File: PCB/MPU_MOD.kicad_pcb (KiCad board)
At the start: 8 copper layers, 45 x 70 mm, 305 parts, among them J1 SJ3-35024K-SMT-TR, J2 2-1734248-0, J501 MEM2090-00-145-00-A_REVA, J701 FTSH-107-01-L-DV-K-A, J801 USB4215-03-A_REVA, J901 73412-0110, U1 IS21ES08GA-JQLI-TR, U201 STC3115IQT, U203 STPMIC1APQR, U3 BQ24298RTWR, U301 STM32MP157FABx, U401 MT41K256M16TW-107_P, U502 HSP051-4M10, U503 HSP051-4M10, U701 HSP051-4M10, U702 HSP051-4M10, U801 FUSB302BMPX, U802 HSP051-4M10, U901 LBEE5PK2AE-771, Y601 NX2012SA-32.768K, Y701 ECS-2520MVQ-240

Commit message: PCD_UPDATE
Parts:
- moved J1 2.37 mm to (110.2, 96.8)
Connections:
- U401 pad H7: /DDR/DDR_DQ14 -> /DDR/DDR_DQ11
- U401 pad H8: /DDR/DDR_DQ11 -> /DDR/DDR_DQ14
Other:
- board size 45 x 70 mm -> 43.5 x 70 mm
- board text added: "move usb"

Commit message: PCB_UPDATE
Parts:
- removed J801: USB4215-03-A_REVA, lib:GCT_USB4215-03-A_REVA
- added J3: USB4510-03-1-A_REVA, lib:GCT_USB4510-03-1-A_REVA, F.Cu at (90.2, 99.4)
- D801: moved to B.Cu
- J1: value SJ3-35024K-SMT-TR -> SJ-43504-SMT-TR; footprint lib:SAMESKY_SJ3-35024K-SMT-TR -> lib:CUI_SJ-43504-SMT-TR
- moved C204 27.9 mm to (47.8, 88.6)
- moved C205 27.9 mm to (45.8, 88.6)
- moved R201 27.9 mm to (46.8, 82.5)
- moved R209 27.9 mm to (44.8, 88.6)
- moved R210 27.9 mm to (46.8, 88.6)
- moved R212 27.9 mm to (42.6, 85.7)
- moved U201 27.9 mm to (45.3, 85.7)
- moved BT201 27.9 mm to (43.2, 88.6)
- moved R202 27.9 mm to (46.8, 83.5)
- moved TH201 27.9 mm to (43.2, 90.9)
- moved TP203 27.9 mm to (47.7, 86.0)
- moved R219 13.6 mm to (83.9, 92.3), turned to -90 degrees
- moved R216 13.3 mm to (87.1, 92.3), turned to -90 degrees
- moved R218 13.3 mm to (85.2, 92.3), turned to 90 degrees
- moved R217 13.2 mm to (86.2, 92.3), turned to 90 degrees
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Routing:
- net /DDR/DDR_A15: track 13.5 -> 1.08 mm
- net /DDR/DDR_CSN: track 30.8 -> 27.1 mm
- net /DDR/DDR_A3: track 25.6 -> 23.7 mm
- net /DDR/DDR_A4: track 23.1 -> 24.5 mm
- net /DDR/DDR_BA2: track 30.7 -> 29.4 mm
- net /DDR/DDR_A0: track 28.6 -> 27.4 mm
- net /DDR/DDR_RASN: track 29.6 -> 28.5 mm
- net /DDR/DDR_A6: track 25.3 -> 26.2 mm
- net /DDR/DDR_A2: track 27.3 -> 26.5 mm
- net /DDR/DDR_A14: track 22.4 -> 23.2 mm
- net /DDR/DDR_A7: track 24.4 -> 25.2 mm
- net /DDR/DDR_A11: track 26.9 -> 27.6 mm
- net /DDR/DDR_CASN: track 32.5 -> 31.8 mm
- net /DDR/DDR_BA0: track 26.1 -> 26.8 mm
- net /DDR/DDR_A8: track 22.6 -> 23.2 mm
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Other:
- board text removed: "move usb"

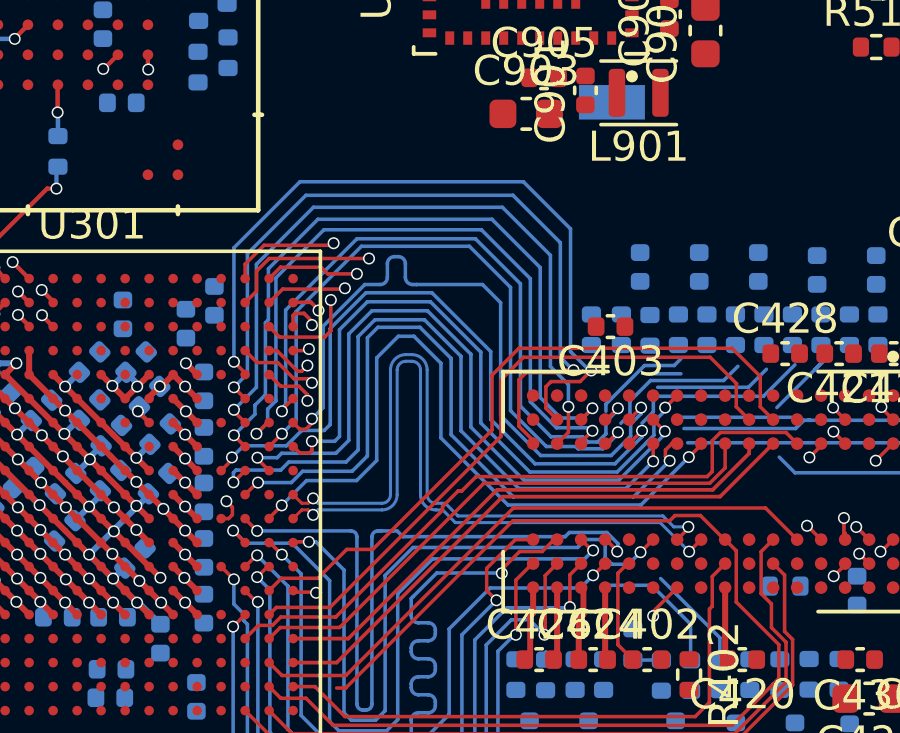
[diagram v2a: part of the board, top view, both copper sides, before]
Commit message: DDR almost done, but it can make GND  T1
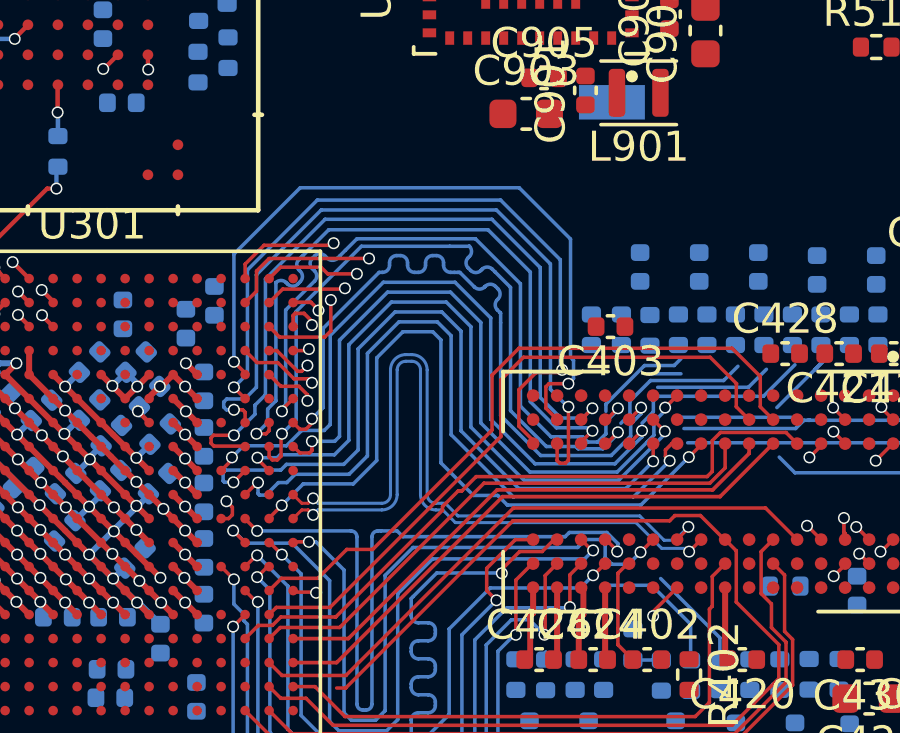
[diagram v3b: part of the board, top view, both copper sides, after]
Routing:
- net /DDR/DDR_A9: track 23.8 -> 25.7 mm
- net /DDR/DDR_A0: track 27.4 -> 29.1 mm
- net /DDR/DDR_A13: track 25.9 -> 24.4 mm
- net /DDR/DDR_A5: track 24.0 -> 25.5 mm
- net /DDR/DDR_A7: track 25.2 -> 24.0 mm
- net /DDR/DDR_WEN: track 32.0 -> 33.2 mm
- net /DDR/DDR_RASN: track 28.5 -> 29.6 mm
- net /DDR/DDR_CASN: track 31.8 -> 32.6 mm
- net /DDR/DDR_A2: track 26.5 -> 27.3 mm
- net /DDR/DDR_BA2: track 29.4 -> 30.2 mm
- net /DDR/DDR_A3: track 23.7 -> 24.4 mm
- net /DDR/DDR_ODT: track 25.1 -> 25.7 mm
- net /DDR/DDR_BA0: track 26.8 -> 27.4 mm
- net /DDR/DDR_CSN: track 27.1 -> 27.6 mm
